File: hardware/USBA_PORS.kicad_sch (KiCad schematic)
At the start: 33 parts, among them J3 0483930003, J4 0483930003, J5 0483930003, J6 0483930003, U13 USB5926C

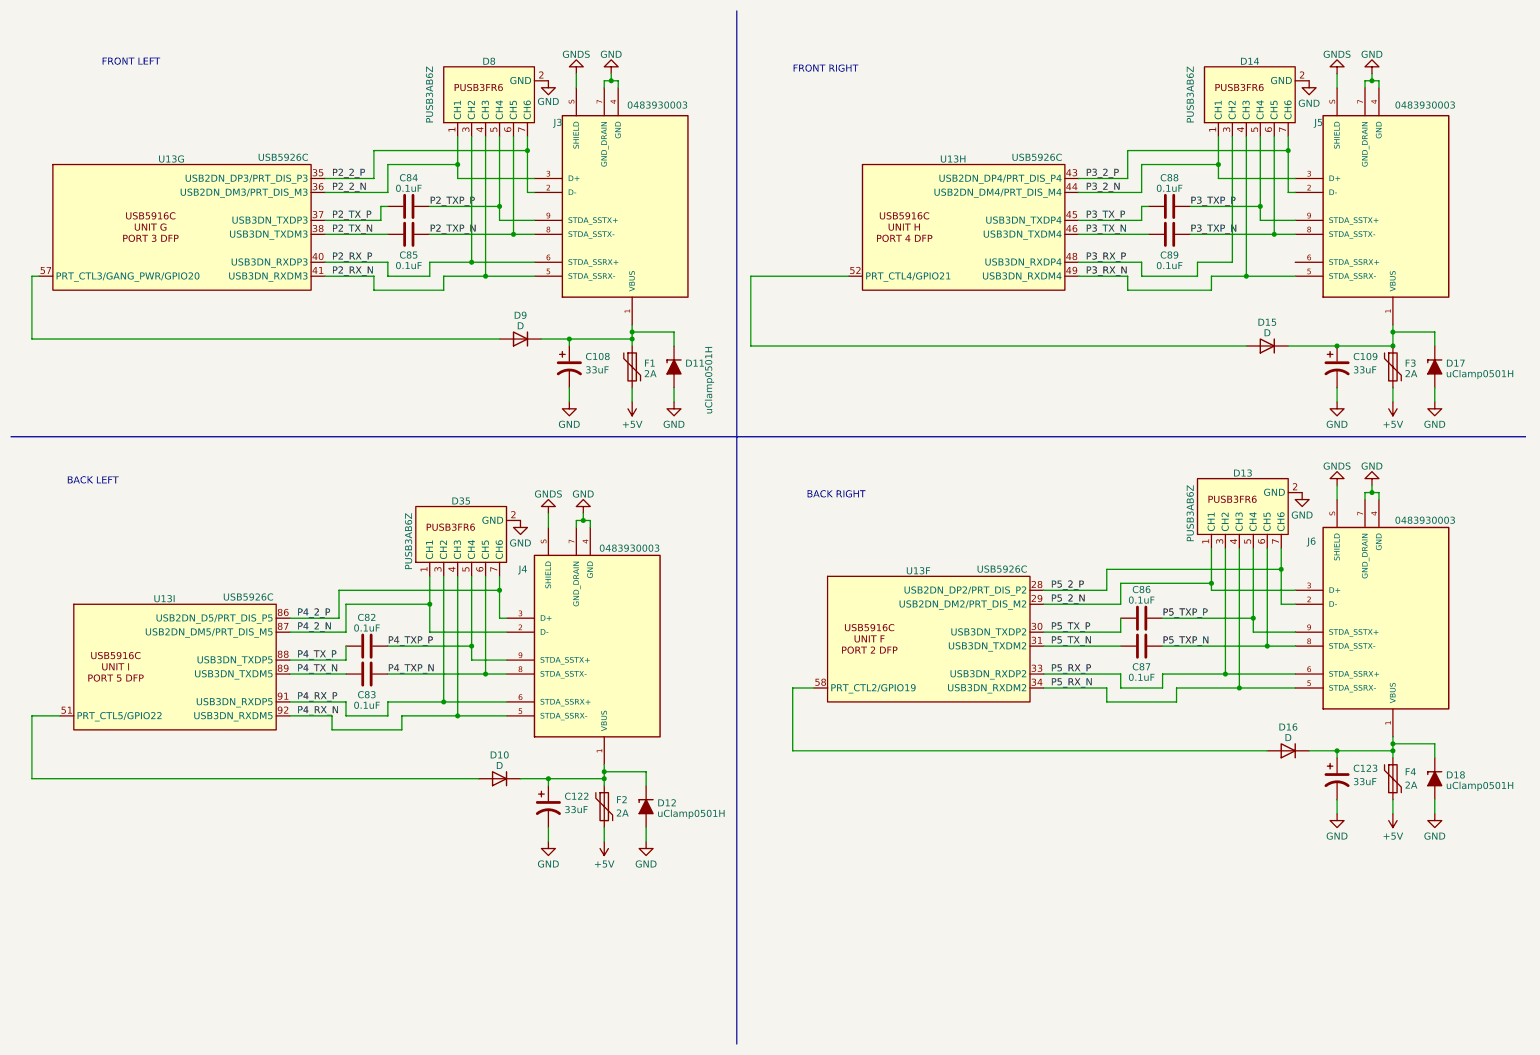
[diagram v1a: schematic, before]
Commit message: migrated to the esp32-s2 and starting new board revison
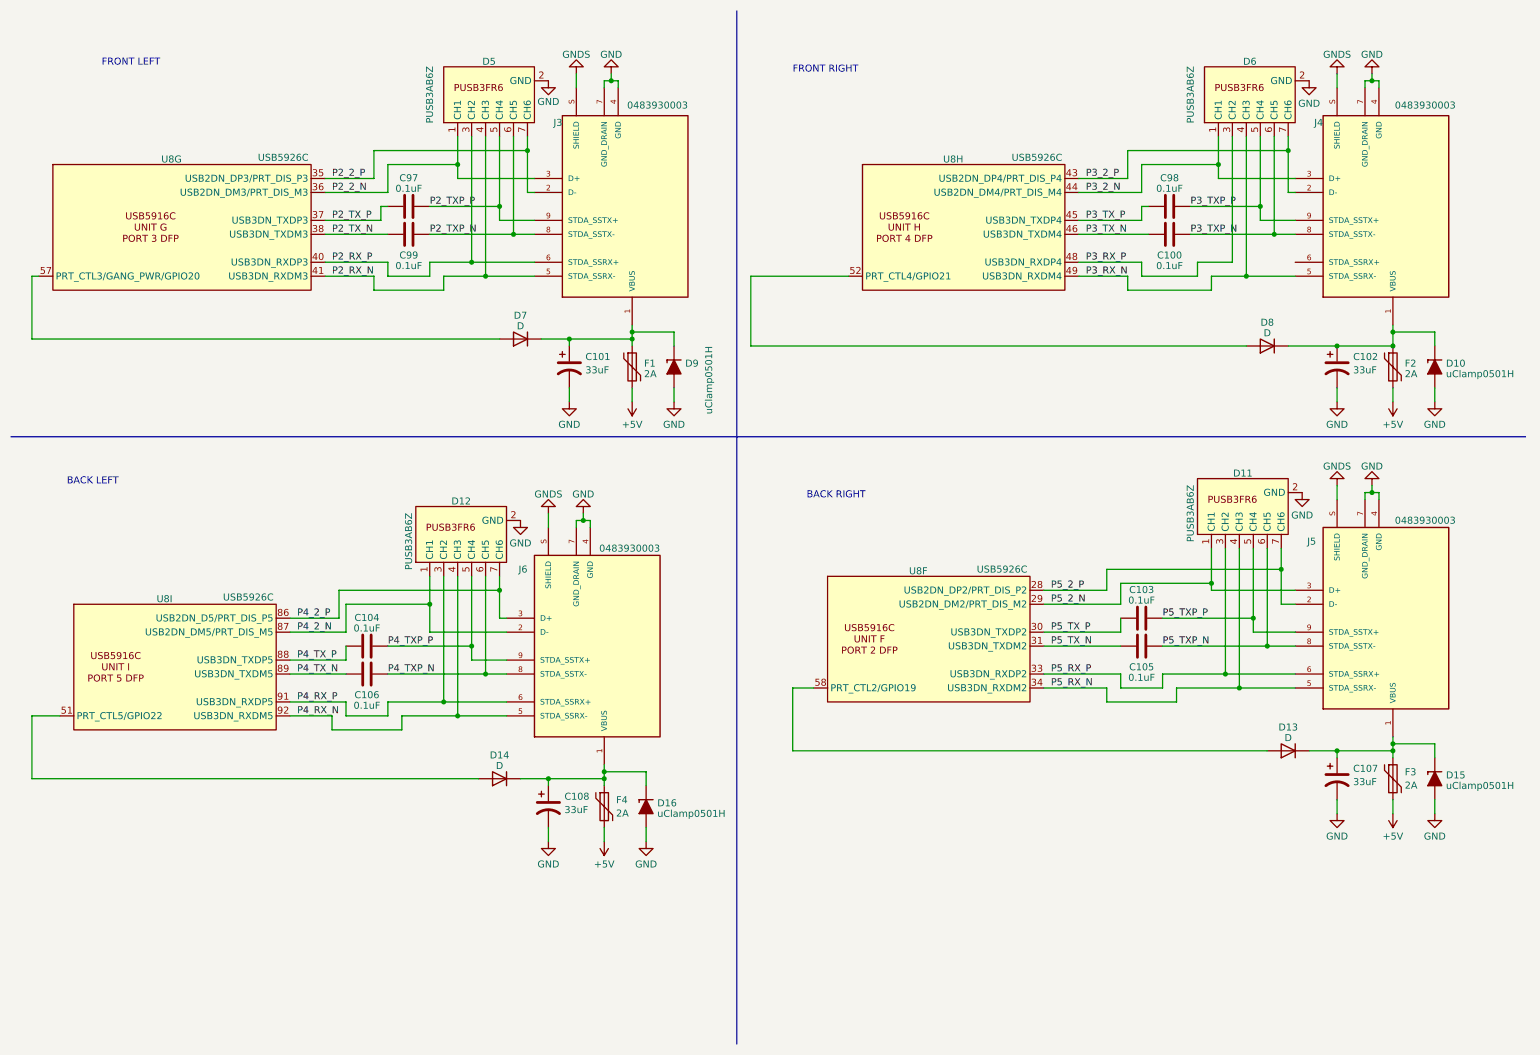
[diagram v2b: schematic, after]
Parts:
- J3: footprint 0483930003:MOLEX_0483930003 -> CARTHING:MOLEX_0483930003
- J4: renamed from J5; footprint 0483930003:MOLEX_0483930003 -> CARTHING:MOLEX_0483930003
- J5: renamed from J6; footprint 0483930003:MOLEX_0483930003 -> CARTHING:MOLEX_0483930003
- J6: renamed from J4; footprint 0483930003:MOLEX_0483930003 -> CARTHING:MOLEX_0483930003
- renumbered C89 to C100, C108 to C101, C109 to C102, C86 to C103, C82 to C104, C87 to C105, C83 to C106, C123 to C107, C122 to C108, C84 to C97, C88 to C98, C85 to C99, D17 to D10, D13 to D11, D35 to D12, D16 to D13, D10 to D14, D18 to D15, D12 to D16, D8 to D5, D14 to D6, D9 to D7, D15 to D8, D11 to D9, F3 to F2, F4 to F3, F2 to F4, U13 to U8
